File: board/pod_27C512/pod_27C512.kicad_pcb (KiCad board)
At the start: 2 copper layers, 39.4 x 57.2 mm, 13 parts, among them J1 EXT_D, J2 EXT_ADDR, J3 VCC_Probe, J4 GND_Probe, J5 ROM Lines, U1 74HCT02

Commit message: Update the 27C512 pod by adding a protection diode
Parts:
- added D3: BAT48ZFILM, Diode_SMD:D_SOD-123, F.Cu at (165.7, 86.4)
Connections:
- J5 pad 2: /EXT_VCC -> Net-(D3-Pad2)
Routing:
- net /EXT_VCC: track 65.1 -> 19.4 mm
- net Net-(D3-Pad2): track 0.00 -> 43.4 mm
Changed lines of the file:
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@@
-(kicad_pcb (version 20171130) (host pcbnew 5.1.8-1.fc33)
+(kicad_pcb (version 20171130) (host pcbnew 5.1.8-4.fc33)
   (general
     (thickness 1.6)
     (drawings 40)
-    (tracks 534)
+    (tracks 536)
     (zones 0)
-    (modules 13)
-    (nets 36)
+    (modules 14)
+    (nets 37)
   )
   (page A4)
@@
   (net 34 "Net-(U1-Pad4)")
   (net 35 "Net-(U1-Pad1)")
+  (net 36 "Net-(D3-Pad2)")
   (net_class Default "This is the default net class."
     (clearance 0.2)
@@
     (add_net /~SAFE_CE)
     (add_net "Net-(D2-Pad2)")
+    (add_net "Net-(D3-Pad2)")
     (add_net "Net-(U1-Pad1)")
     (add_net "Net-(U1-Pad4)")
@@
     (add_net "Net-(D1-Pad2)")
     (add_net VCC)
+  )
+  (module Diode_SMD:D_SOD-123 (layer F.Cu)
+    (at 165.735 86.36 45)
+    (descr SOD-123)
+    (tags SOD-123)
+    (attr smd)
+    (fp_text reference D3 (at 0 0 45) (layer F.SilkS)
+      (effects (font (size 1 1) (thickness 0.15)))
+    )
+    (fp_text value BAT48ZFILM (at 0 2.1 45) (layer F.Fab)
+      (effects (font (size 1 1) (thickness 0.15)))
+    )
+    (fp_line (start -2.25 -1) (end 1.65 -1) (layer F.SilkS) (width 0.12))
+    (fp_line (start -2.25 1) (end 1.65 1) (layer F.SilkS) (width 0.12))
+    (fp_line (start -2.35 -1.15) (end -2.35 1.15) (layer F.CrtYd) (width 0.05))
+    (fp_line (start 2.35 1.15) (end -2.35 1.15) (layer F.CrtYd) (width 0.05))
+    (fp_line (start 2.35 -1.15) (end 2.35 1.15) (layer F.CrtYd) (width 0.05))
+    (fp_line (start -2.35 -1.15) (end 2.35 -1.15) (layer F.CrtYd) (width 0.05))
+    (fp_line (start -1.4 -0.9) (end 1.4 -0.9) (layer F.Fab) (width 0.1))
+    (fp_line (start 1.4 -0.9) (end 1.4 0.9) (layer F.Fab) (width 0.1))
+    (fp_line (start 1.4 0.9) (end -1.4 0.9) (layer F.Fab) (width 0.1))
+    (fp_line (start -1.4 0.9) (end -1.4 -0.9) (layer F.Fab) (width 0.1))
+    (fp_line (start -0.75 0) (end -0.35 0) (layer F.Fab) (width 0.1))
+    (fp_line (start -0.35 0) (end -0.35 -0.55) (layer F.Fab) (width 0.1))
+    (fp_line (start -0.35 0) (end -0.35 0.55) (layer F.Fab) (width 0.1))
+    (fp_line (start -0.35 0) (end 0.25 -0.4) (layer F.Fab) (width 0.1))
+    (fp_line (start 0.25 -0.4) (end 0.25 0.4) (layer F.Fab) (width 0.1))
+    (fp_line (start 0.25 0.4) (end -0.35 0) (layer F.Fab) (width 0.1))
+    (fp_line (start 0.25 0) (end 0.75 0) (layer F.Fab) (width 0.1))
+    (fp_line (start -2.25 -1) (end -2.25 1) (layer F.SilkS) (width 0.12))
+    (fp_text user %R (at 0 -2 45) (layer F.Fab)
+      (effects (font (size 1 1) (thickness 0.15)))
+    )
+    (pad 2 smd rect (at 1.65 0 45) (size 0.9 1.2) (layers F.Cu F.Paste F.Mask)
+      (net 36 "Net-(D3-Pad2)"))
+    (pad 1 smd rect (at -1.65 0 45) (size 0.9 1.2) (layers F.Cu F.Paste F.Mask)
+      (net 33 /EXT_VCC))
+    (model ${KISYS3DMOD}/Diode_SMD.3dshapes/D_SOD-123.wrl
+      (at (xyz 0 0 0))
+      (scale (xyz 1 1 1))
+      (rotate (xyz 0 0 0))
+    )
   )
   (module Package_SO:SO-14_3.9x8.65mm_P1.27mm (layer B.Cu)
@@
       (net 19 /A12))
     (pad 2 thru_hole oval (at 2.54 0) (size 1.7 1.7) (drill 1) (layers *.Cu *.Mask)
-      (net 33 /EXT_VCC))
+      (net 36 "Net-(D3-Pad2)"))
     (pad 1 thru_hole rect (at 0 0) (size 1.7 1.7) (drill 1) (layers *.Cu *.Mask)
       (net 16 /A15))
@@
   (via (at 160.5346 71.5384) (size 0.8) (layers F.Cu B.Cu) (net 32))
   (segment (start 162.7525 87.63) (end 162.7525 90.17) (width 0.4) (layer F.Cu) (net 33))
-  (segment (start 165.1 44.4303) (end 165.647 44.4303) (width 0.4) (layer F.Cu) (net 33))
-  (segment (start 165.647 44.4303) (end 167.3307 46.114) (width 0.4) (layer F.Cu) (net 33))
-  (segment (start 167.3307 46.114) (end 167.3307 83.0518) (width 0.4) (layer F.Cu) (net 33))
-  (segment (start 167.3307 83.0518) (end 162.7525 87.63) (width 0.4) (layer F.Cu) (net 33))
   (segment (start 162.7525 87.63) (end 157.6725 87.63) (width 0.4) (layer F.Cu) (net 33))
-  (segment (start 165.1 43.18) (end 165.1 44.4303) (width 0.4) (layer F.Cu) (net 33))
   (segment (start 153.735 83.2035) (end 153.735 82.55) (width 0.4) (layer B.Cu) (net 33))
   (segment (start 153.735 83.82) (end 153.735 83.2035) (width 0.4) (layer B.Cu) (net 33))
@@
   (segment (start 156.7141 87.63) (end 152.2876 83.2035) (width 0.4) (layer F.Cu) (net 33))
   (via (at 152.2876 83.2035) (size 0.8) (layers F.Cu B.Cu) (net 33))
+  (segment (start 162.855774 87.526726) (end 162.7525 87.63) (width 0.4) (layer F.Cu) (net 33))
+  (segment (start 164.568274 87.526726) (end 162.855774 87.526726) (width 0.4) (layer F.Cu) (net 33))
+  (segment (start 167.3307 84.7643) (end 166.901726 85.193274) (width 0.4) (layer F.Cu) (net 36))
+  (segment (start 165.1 44.4303) (end 165.647 44.4303) (width 0.4) (layer F.Cu) (net 36))
+  (segment (start 167.3307 46.114) (end 167.3307 84.7643) (width 0.4) (layer F.Cu) (net 36))
+  (segment (start 165.647 44.4303) (end 167.3307 46.114) (width 0.4) (layer F.Cu) (net 36))
+  (segment (start 165.1 43.18) (end 165.1 44.4303) (width 0.4) (layer F.Cu) (net 36))
   (segment (start 153.735 81.28) (end 154.157 81.28) (width 0.25) (layer B.Cu) (net 34))
   (segment (start 154.157 81.28) (end 156.697 78.74) (width 0.25) (layer B.Cu) (net 34))

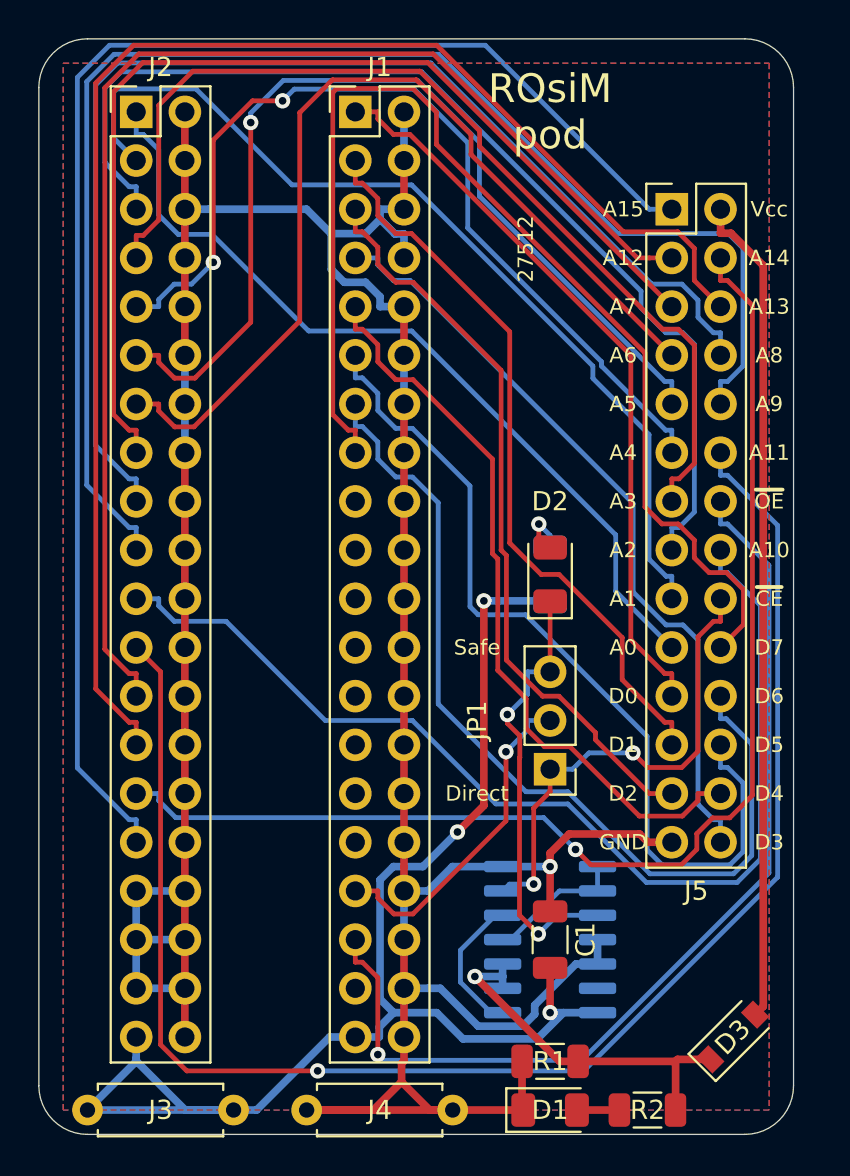
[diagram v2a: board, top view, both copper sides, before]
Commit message: Update 27C512 pod
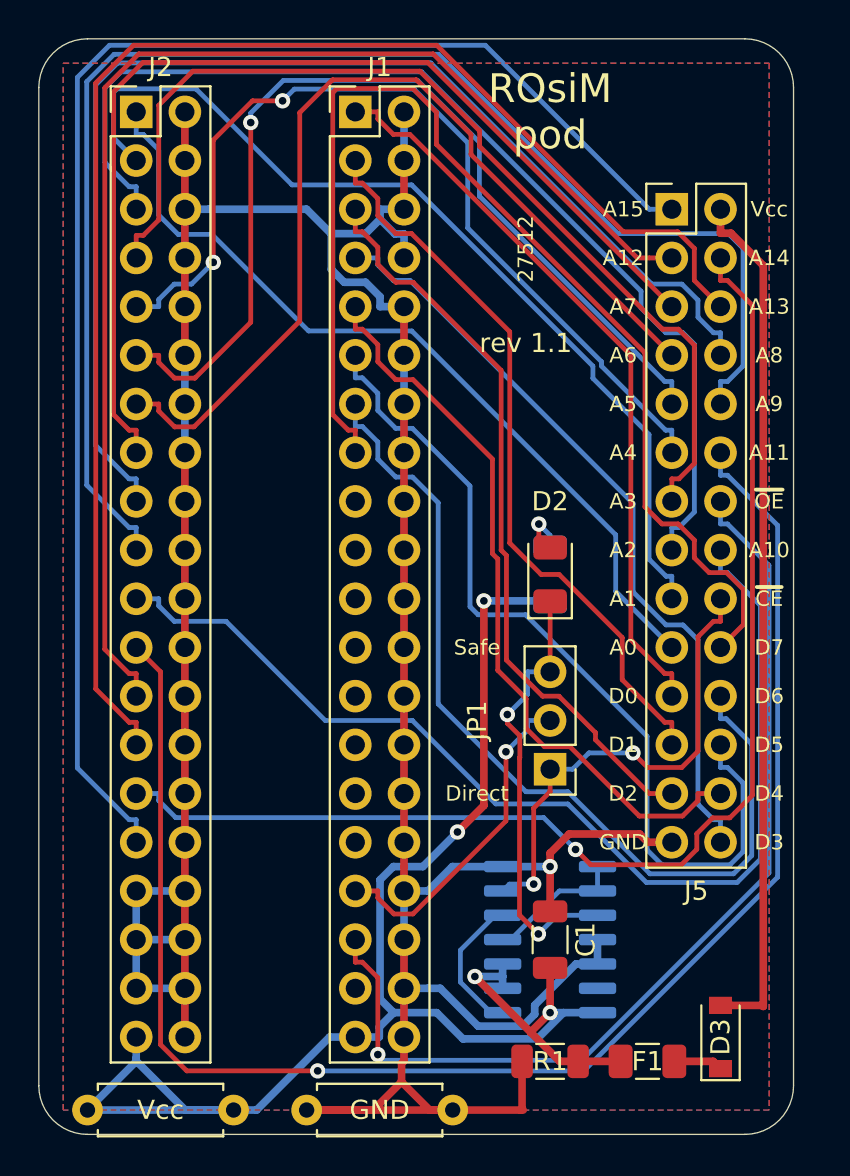
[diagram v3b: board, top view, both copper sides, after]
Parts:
- removed D1: RED, LED_SMD:LED_1206_3216Metric
- removed R2: 1k, Resistor_SMD:R_1206_3216Metric
- added F1: 200mA, Fuse:Fuse_1206_3216Metric, F.Cu at (161.3, 87.6)
- moved D3 0.64 mm to (165.1, 86.4), turned to 90 degrees
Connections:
- D3 pad 1: /EXT_VCC -> Net-(D3-Pad1)
- R1 pad 2: /EXT_VCC -> VCC
- U1 pad 2: /EXT_VCC -> VCC
- U1 pad 3: /EXT_VCC -> VCC
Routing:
- net /EXT_VCC: track 19.4 -> 0.00 mm, vias 1 -> 0
- net VCC: track 72.6 -> 86.2 mm, vias 3 -> 4
- net Net-(D3-Pad1): track 0.00 -> 2.57 mm
- net Net-(D1-Pad2): track 2.22 -> 0.00 mm
- net Net-(D3-Pad2): track 43.4 -> 45.1 mm
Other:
- board text added: "rev 1.1"
